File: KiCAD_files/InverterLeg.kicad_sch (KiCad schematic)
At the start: 94 parts, among them J801 Conn_Coaxial_Small, J802 Conn_Coaxial_Small, J803 Conn_01x01_Pin, J804 Conn_01x03_Socket, J806 Conn_01x01_Pin, J811 Screw_Terminal_01x01, J814 Screw_Terminal_01x01, J817 Screw_Terminal_01x01, J825 HC-PBB08-2-08-M-H4.0-G1-R-P-04, J827 HC-PBB08-2-08-M-H4.0-G1-R-P-04, J831 HC-PBB08-2-08-M-H4.0-G1-R-P-04, Q801 IPT60R055CM8, Q802 IPT60R055CM8, T801 TE1212-2W6ENT, T802 TE1212-2W6ENT, U704 VPS8701B, U707 VPS8701B, U801 LT1761-SD, U802 LT1761-SD, U811 TMP117xxDRV, U815 TMP117xxDRV

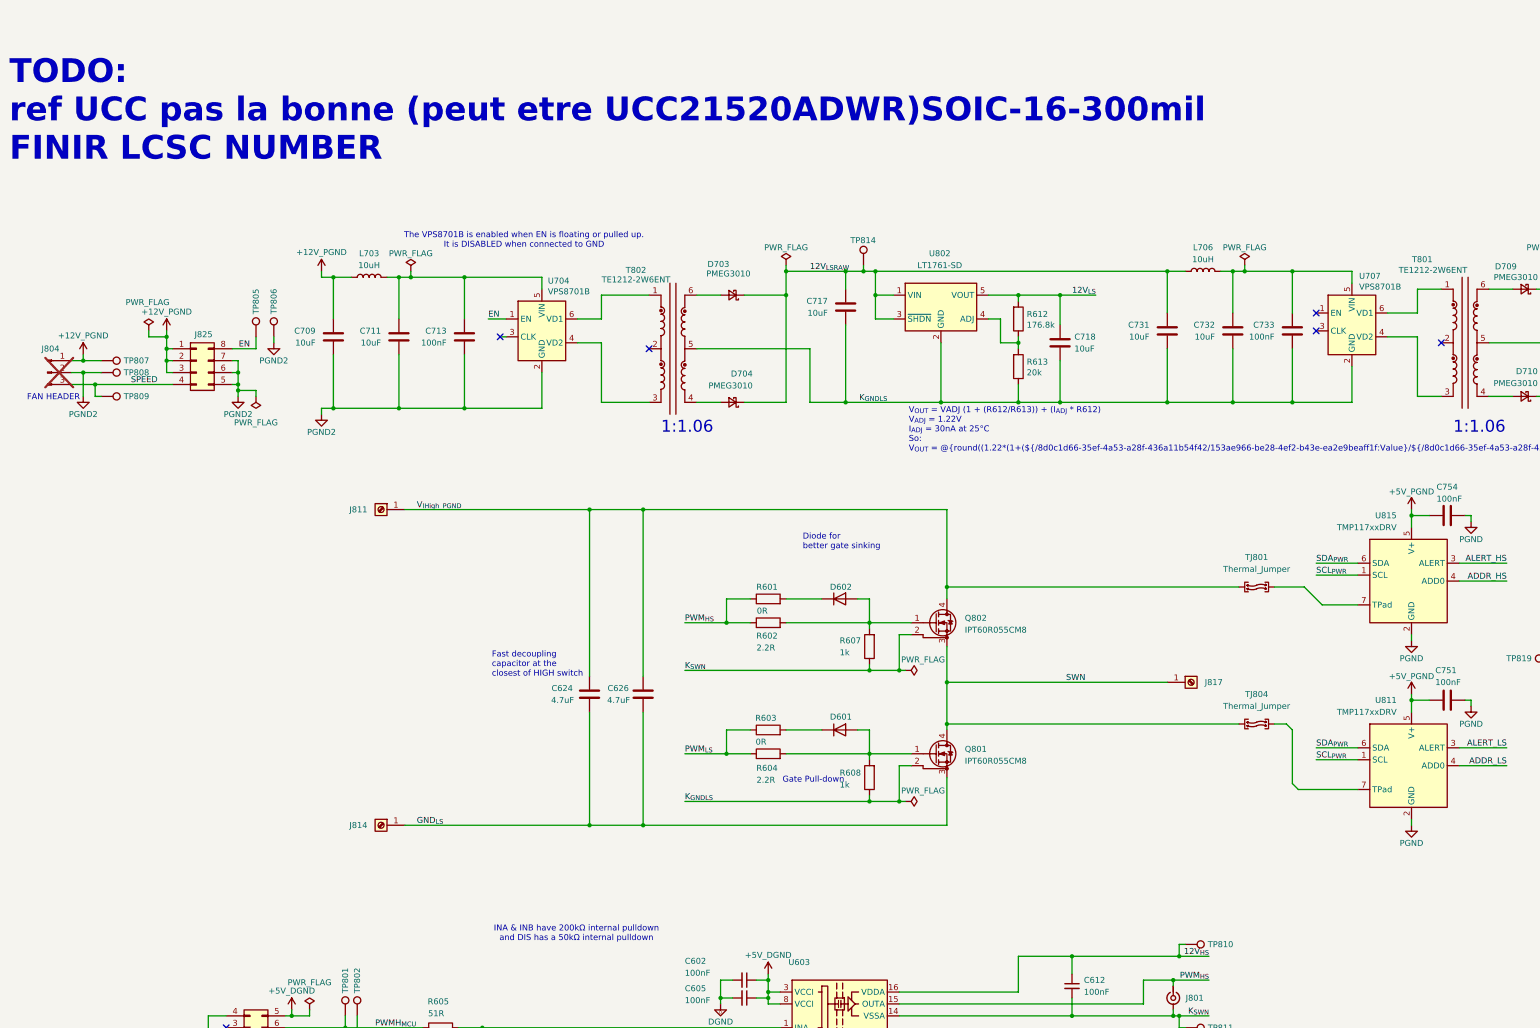
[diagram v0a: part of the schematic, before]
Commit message: added math for grid current and ripple current for ldo
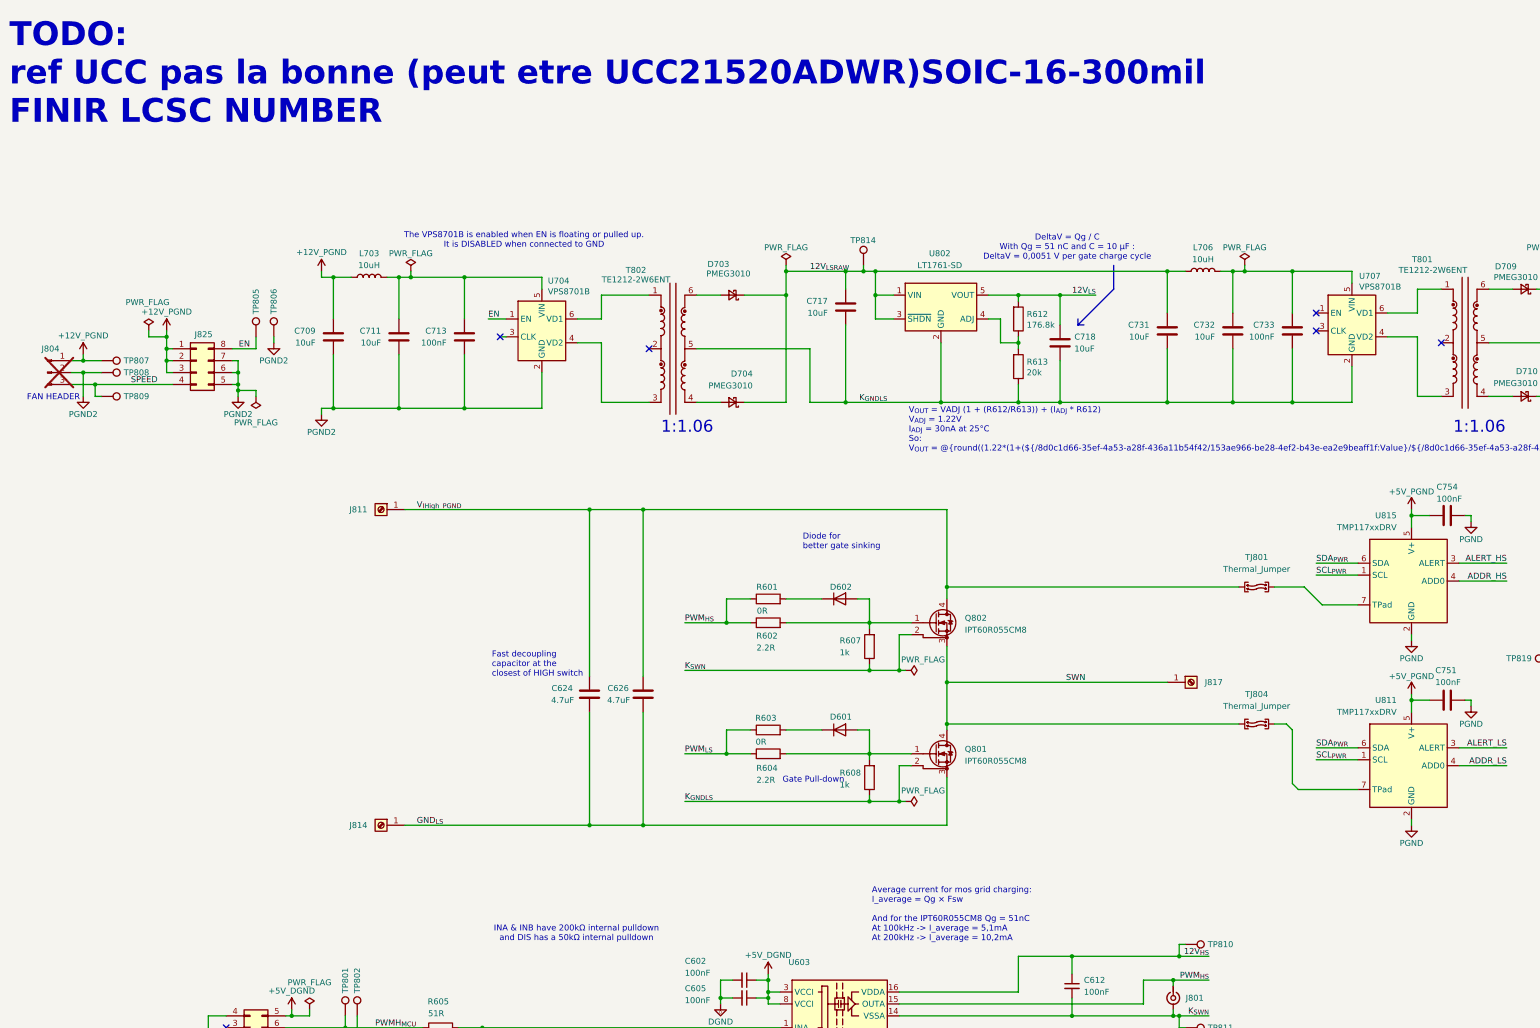
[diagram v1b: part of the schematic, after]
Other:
- note added: "Average current for mos grid charging: I_average = Qg × Fsw And for the IPT60R055CM8 Qg = 51nC At 100kHz -> I_average = 5,1mA At 200kHz -> I_average = 10,2mA"
- note added: "DeltaV = Qg / C With Qg = 51 nC and C = 10 µF : DeltaV = 0,0051 V per gate charge cycle"
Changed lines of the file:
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@@
 	(text "TODO:\nref UCC pas la bonne (peut etre UCC21520ADWR)SOIC-16-300mil\nFINIR LCSC NUMBER"
 		(exclude_from_sim no)
-		(at 10.922 -5.08 0)
+		(at 10.922 -12.954 0)
 		(effects
 			(font
@@
 		)
 	)
+	(text "DeltaV = Qg / C\nWith Qg = 51 nC and C = 10 µF :\nDeltaV = 0,0051 V per gate charge cycle"
+		(exclude_from_sim no)
+		(at 236.474 24.13 0)
+		(effects
+			(font
+				(size 1.27 1.27)
+			)
+		)
+	)
+	(text "Average current for mos grid charging:\nI_average = Qg × Fsw\n\nAnd for the IPT60R055CM8 Qg = 51nC\nAt 100kHz -> I_average = 5,1mA\nAt 200kHz -> I_average = 10,2mA"
+		(exclude_from_sim no)
+		(at 194.818 166.37 0)
+		(effects
+			(font
+				(size 1.27 1.27)
+			)
+			(justify left)
+		)
+	)
 	(text "1:1.06"
 		(exclude_from_sim no)
@@
 		)
 	)
+	(polyline
+		(pts
+			(xy 238.76 39.37) (xy 238.76 40.64)
+		)
+		(stroke
+			(width 0)
+			(type default)
+		)
+	)
 	(wire
 		(pts
@@
 		)
 	)
+	(polyline
+		(pts
+			(xy 246.38 27.94) (xy 246.38 33.02)
+		)
+		(stroke
+			(width 0)
+			(type default)
+		)
+	)
 	(wire
 		(pts
@@
 		)
 	)
+	(polyline
+		(pts
+			(xy 246.38 33.02) (xy 238.76 40.64)
+		)
+		(stroke
+			(width 0)
+			(type default)
+		)
+	)
 	(wire
 		(pts
@@
 		)
 		(stroke
+			(width 0)
+			(type default)
+		)
+	)
+	(polyline
+		(pts
+			(xy 238.76 40.64) (xy 240.03 40.64)
+		)
+		(stroke

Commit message: Added missing LCSC numbers & rotPos. Fixed DRC rules. Moved logo out of galva iso. Revert GND plane modif.
Signed-off-by: Jean Alinei <jean.alinei@owntech.org>
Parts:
- C602, C605, C607, C608, C612, C614: LCSC (none) -> C14663; Package 0805 -> (none); Voltage 50V -> (none); manf# C0805C104K5RACTU -> (none)
- C604, C703: LCSC (none) -> C1648; Package 0805 -> (none); Voltage 50V -> (none); manf# CC0805JRNPO9BN200 -> (none)
- C616: footprint Capacitor_SMD:C_1206_3216Metric -> Capacitor_SMD:C_0805_2012Metric; LCSC (none) -> C440198; Package 1210 -> (none); Voltage 50V -> (none); manf# 12105C106KAT2A -> (none)
- C624, C626: value 4.7uF -> 3.3uF; LCSC (none) -> C22370027; Package 1210 -> (none); Voltage 100V -> (none); manf# 12101C475K4T2A -> (none)
- C709, C711, C717, C718, C719, C731, C732, C734: LCSC (none) -> C440198
- C713, C733, C751, C754: LCSC (none) -> C14663
- D601: value PMEG3010CEJ,115 -> PMEG4010; LCSC C28646370 -> C478156; manf# PMEG2010AEJ,115 -> (none)
- D602: value (none) -> PMEG4010; LCSC C28646370 -> C478156
- D703, D704, D709, D710: value PMEG3010 -> PMEG4010; LCSC C28646370 -> C478156
- J803, J806: value Conn_01x01_Pin -> (none)
- Q801, Q802: value IPT60R055CM8 -> (none); LCSC C47146866 -> C18221382; Position Offset (none) -> -1.27,0; Rotation Offset (none) -> 270
- R601, R603: value 0R -> 1R; LCSC (none) -> C22936; Package 0805 -> (none); Power 0.125W -> (none); manf# CR0805AF/-2R20EAS -> (none)
- R602, R604: value 2.2R -> 1R; LCSC (none) -> C22936; Package 0805 -> (none); Power 0.125W -> (none); manf# CR0805AF/-2R20EAS -> (none)
- R605, R606: LCSC (none) -> C23197; Package 0805 -> (none); Voltage 150V -> (none); manf# CR0805-FX-51R0ELF -> (none)
- R607, R608: value 1k -> 10k; LCSC (none) -> C25744; Package 0805 -> (none); Power 0.125W -> (none); manf# RC0805FR-071KP -> (none)
- R609: footprint Resistor_SMD:R_0603_1608Metric -> Resistor_SMD:R_0402_1005Metric; LCSC C4328 -> C25765; Package 0805 -> (none); Power 0.125W -> (none); manf# CR0805-FX-2002ELF -> (none)
- R610, R612: value 176.8k -> 178k; LCSC (none) -> C26995; Package 0805 -> (none); Voltage 150V -> (none); manf# CR0805-FX-51R0ELF -> (none)
- R611, R613: LCSC (none) -> C25765; Package 0805 -> (none); Voltage 150V -> (none); manf# CR0805-FX-51R0ELF -> (none)
- T801, T802: LCSC (none) -> C54443261
- TJ801, TJ804: value Thermal_Jumper -> (none)
- U603: value (none) -> UCC21520; LCSC (none) -> C601651
- U811, U815: Rotation Offset (none) -> 270
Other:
- note added: "UCC21520A Variant has lower UVLO on VDD permitting compatibility with GanFets"
- note removed: "TODO: ref UCC pas la bonne (peut etre UCC21520ADWR)SOIC-16-300mil FINIR LCSC NUMBER"
